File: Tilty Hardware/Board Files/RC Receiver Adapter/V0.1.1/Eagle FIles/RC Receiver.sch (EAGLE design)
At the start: 33 parts, among them J1 AVR_SPI_PRG_6PTH, Q1 16MHz, U1 ATMEGA328P, U2 L298_BRIDGE_DRIVER, U3 LM2931

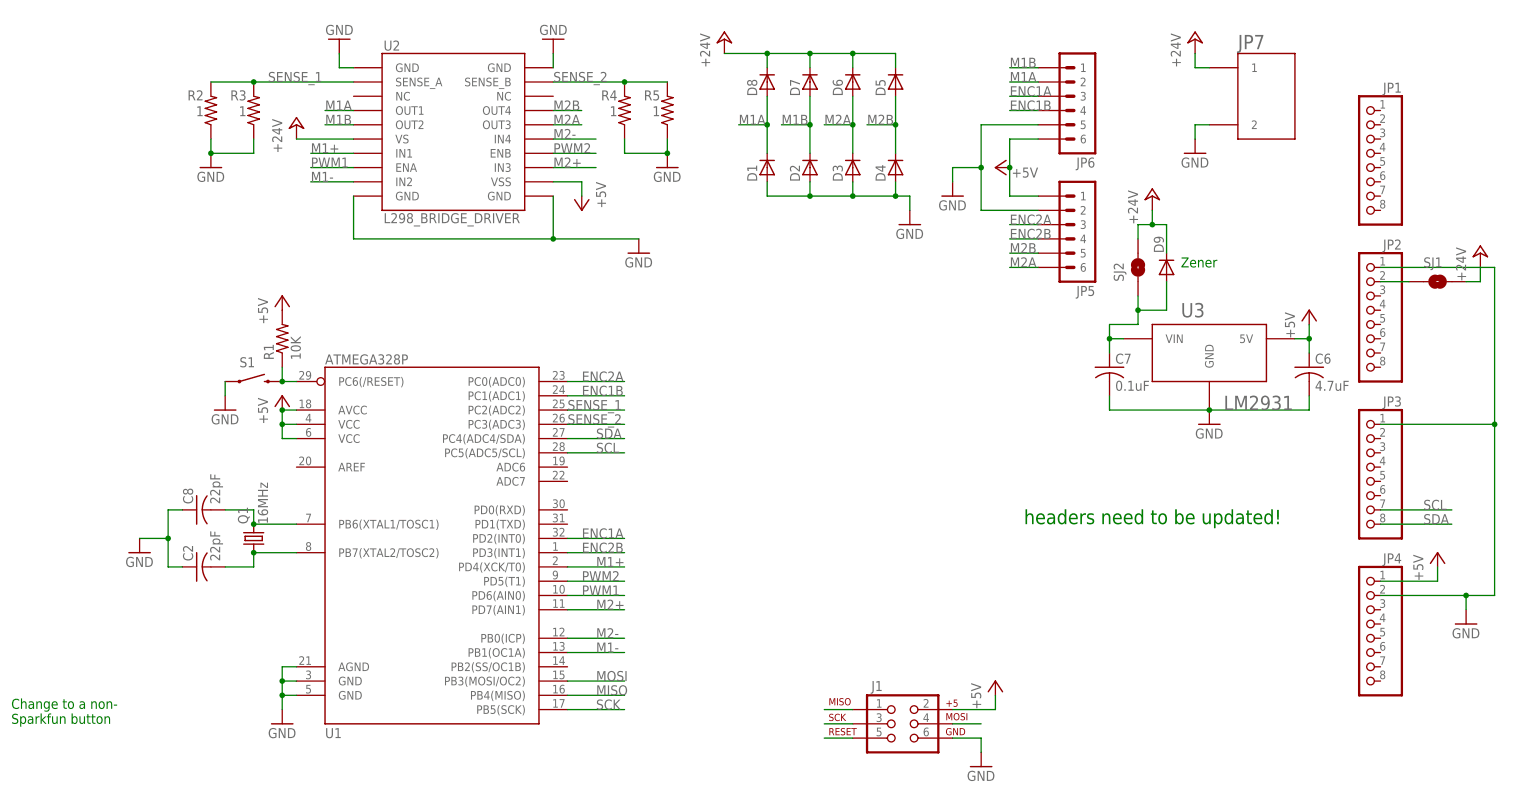
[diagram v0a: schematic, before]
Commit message: New RC Receiver add-on testing code and minor motor driver updates
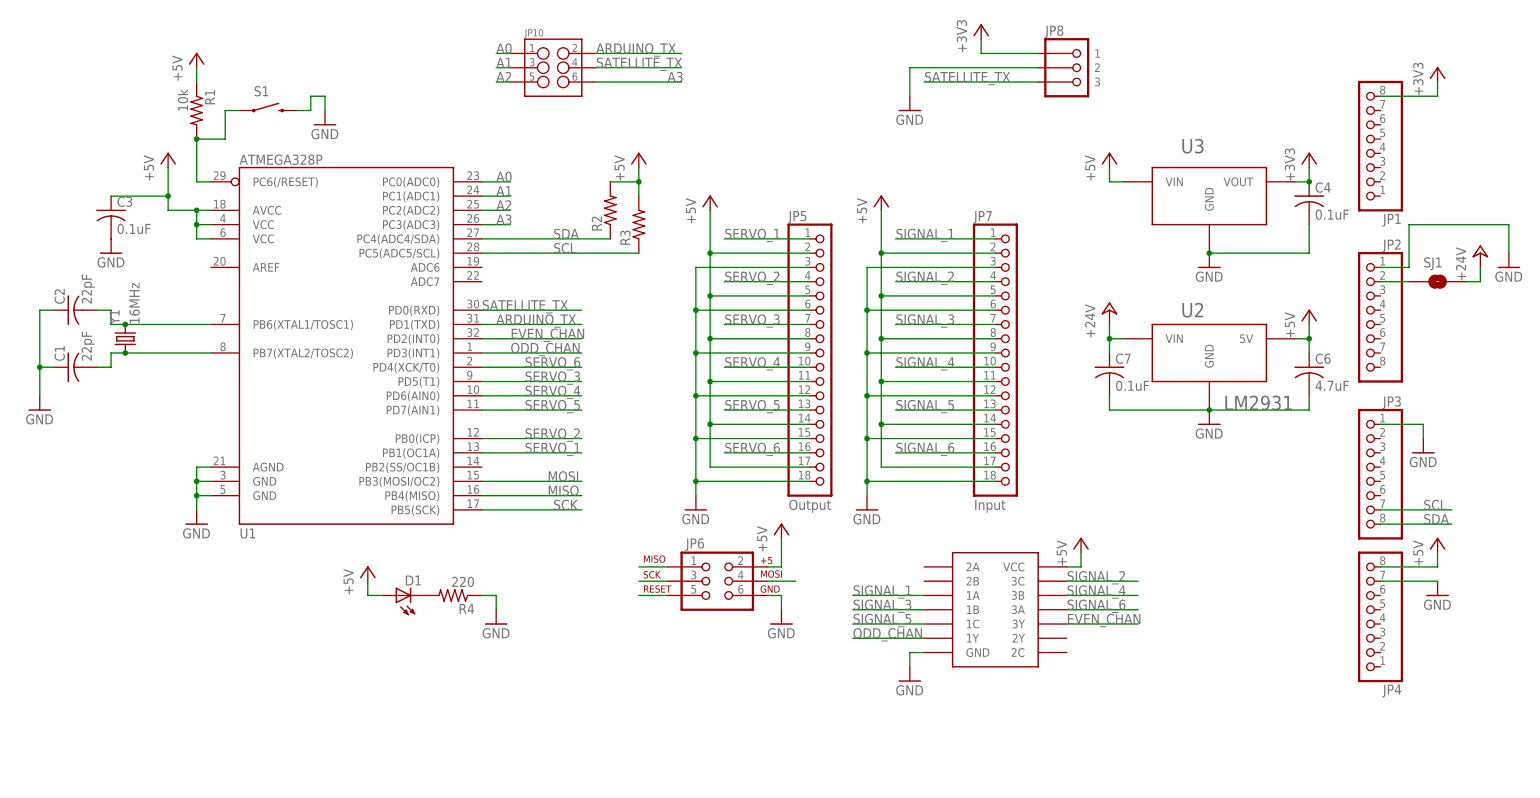
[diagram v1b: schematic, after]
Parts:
- removed C8: 22pF, resistor:C-USC0603
- removed D2, D3, D4, D5, D6, D7, D8: (no value), semicon-smd-ipc:D-SOD123
- removed D9: (no value), diode:DIODE-DO214AA
- removed J1: AVR_SPI_PRG_6PTH, SparkFun-Connectors:AVR_SPI_PRG_6PTH
- removed Q1: 16MHz, crystal:CRYSTALCTS406
- removed R5: 1, resistor:R-US_R0603
- removed SJ2: SOLDERJUMPERTRACE, SparkFun-Passives:SOLDERJUMPERTRACE
- added C1: 22pF, resistor:C-USC0603
- added C3, C4: 0.1uF, resistor:C-USC0603
- added JP10: (no value), SparkFun-Connectors:M03X2NO_SILK
- added JP8: 3-PIN_JST_ZH_PTH_CONNECTORRIGHT_ANGLE_PTH, My Parts:3-PIN_JST_ZH_PTH_CONNECTORRIGHT_ANGLE_PTH
- added U4: C74HC407514-SOIC, My Parts:C74HC407514-SOIC
- added Y1: 16MHz, SparkFun-FreqCtrl:CRYSTAL5X3
- D1: device semicon-smd-ipc:D-SOD123 -> SparkFun-LED:LED-GREENLED-0805_NO_SILK; PART# CDBW140-G -> (none)
- JP5: value 6PIN-SH_RIGHT_ANGLE -> Output; device con-jst:6PIN-SH_RIGHT_ANGLE -> My Parts:18_PIN_HEADER3X6_PTH_HEADER; PART# SM06B-SRSS-TB(LF)(SN) -> (none)
- JP6: value 6PIN-SH_RIGHT_ANGLE -> AVR_SPI_PRG_62X3_LOCK; device con-jst:6PIN-SH_RIGHT_ANGLE -> SparkFun-Connectors:AVR_SPI_PRG_62X3_LOCK; PART# SM06B-SRSS-TB(LF)(SN) -> (none)
- JP7: value 2-POS_SMD_TERM_BLOCK -> Input; device My Parts:2-POS_SMD_TERM_BLOCK -> My Parts:18_PIN_HEADER3X6_PTH_HEADER
- R1: value 10K -> 10k
- R2, R3: value 1 -> (none)
- R4: value 1 -> 220
- U2: value L298_BRIDGE_DRIVER -> LM2931; device SparkFun-PowerIC:L298_BRIDGE_DRIVER -> on-semiconductor:LM2931; PART# (none) -> lm2931
- U3: value LM2931 -> AP7313SOT23R; device on-semiconductor:LM2931 -> My Parts:AP7313SOT23R
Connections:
- removed net ENC1A: JP6.3, U1.PD2(INT0)
- removed net ENC1B: JP6.4, U1.PC1(ADC1)
- removed net ENC2A: JP5.3, U1.PC0(ADC0)
- removed net ENC2B: JP5.4, U1.PD3(INT1)
- removed net M1+: U1.PD4(XCK/T0), U2.IN1
- removed net M1-: U1.PB1(OC1A), U2.IN2
- removed net M1A: D1.C, D8.A, JP6.2, U2.OUT1
- removed net M1B: D2.C, D7.A, JP6.1, U2.OUT2
- removed net M2+: U1.PD7(AIN1), U2.IN3
- removed net M2-: U1.PB0(ICP), U2.IN4
- removed net M2A: D3.C, D6.A, JP5.6, U2.OUT3
- removed net M2B: D4.C, D5.A, JP5.5, U2.OUT4
- removed net N$3: C7.1, D9.A, SJ2.1, U3.VIN
- removed net N$6: C8.2, Q1.2, U1.PB6(XTAL1/TOSC1)
- removed net N$7: C2.2, Q1.1, U1.PB7(XTAL2/TOSC2)
- removed net PWM1: U1.PD6(AIN0), U2.ENA
- removed net PWM2: U1.PD5(T1), U2.ENB
- removed net SENSE_1: R2.2, R3.2, U1.PC2(ADC2), U2.SENSE_A
- removed net SENSE_2: R4.2, R5.2, U1.PC3(ADC3), U2.SENSE_B
- new net +3V3: C4.1, JP1.8, JP8.1, U3.VOUT
- new net A0: JP10.1, U1.PC0(ADC0)
- new net A1: JP10.3, U1.PC1(ADC1)
- new net A2: JP10.5, U1.PC2(ADC2)
- new net A3: JP10.6, U1.PC3(ADC3)
- new net ARDUINO_TX: JP10.2, U1.PD1(TXD)
- new net EVEN_CHAN: U1.PD2(INT0), U4.3Y
- new net N$1: C2.2, U1.PB6(XTAL1/TOSC1), Y1.2
- new net N$2: C1.2, U1.PB7(XTAL2/TOSC2), Y1.1
- new net N$8: D1.C, R4.2
- new net ODD_CHAN: U1.PD3(INT1), U4.1Y
- new net SATELLITE_TX: JP10.4, JP8.3, U1.PD0(RXD)
- new net SERVO_1: JP5.1, U1.PB1(OC1A)
- new net SERVO_2: JP5.4, U1.PB0(ICP)
- new net SERVO_3: JP5.7, U1.PD5(T1)
- new net SERVO_4: JP5.10, U1.PD6(AIN0)
- new net SERVO_5: JP5.13, U1.PD7(AIN1)
- new net SERVO_6: JP5.16, U1.PD4(XCK/T0)
- new net SIGNAL_1: JP7.1, U4.1A
- new net SIGNAL_2: JP7.4, U4.3C
- new net SIGNAL_3: JP7.7, U4.1B
- new net SIGNAL_4: JP7.10, U4.3B
- new net SIGNAL_5: JP7.13, U4.1C
- new net SIGNAL_6: JP7.16, U4.3A
- net +24V: now also C7.1, U2.VIN; no longer D5.C, D6.C, D7.C, D8.C, D9.C, JP7.1, SJ2.2, U2.VS
- net +5V: now also C3.1, D1.A, JP4.8, JP5.11, JP5.14, JP5.17, JP5.2, JP5.5, JP5.8, JP6.2, JP7.11, JP7.14, JP7.17, JP7.2, JP7.5, JP7.8, R1.1, R2.2, R3.2, U2.5V, U3.VIN, U4.VCC; no longer J1.2, JP4.1, JP5.1, JP6.6, R1.2, U2.VSS, U3.5V
- net GND: now also C1.1, C3.2, C4.2, JP4.7, JP5.12, JP5.15, JP5.18, JP5.3, JP5.6, JP5.9, JP6.6, JP7.12, JP7.15, JP7.18, JP7.3, JP7.6, JP7.9, JP8.2, S1.2, U2.GND, U4.GND; no longer C8.1, D1.A, D2.A, D3.A, D4.A, J1.6, JP4.2, JP5.2, JP6.5, JP7.2, R2.1, R3.1, R5.1, S1.1, U2.GND@1, U2.GND@10, U2.GND@11, U2.GND@20
- net MISO: now also JP6.1; no longer J1.1
- net MOSI: now also JP6.4; no longer J1.4
- net RESET: now also JP6.5, R1.2, S1.1; no longer J1.5, R1.1, S1.2
- net SCK: now also JP6.3; no longer J1.3
- net SCL: now also R3.1
- net SDA: now also R2.1
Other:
- note removed: "Change to a non- Sparkfun button"
- note removed: "Zener"
- note removed: "headers need to be updated!"
- moved on the sheet: C2, JP1, JP4, R1, R2, R3, R4, S1, U1, U3

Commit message: R/C Receiver add-on work
fixed OR gate, moved reset button, corrected servo labels
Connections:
- net EVEN_CHAN: now also U1.PD3(INT1), U4.1Y; no longer U1.PD2(INT0), U4.3Y
- net ODD_CHAN: now also U1.PD2(INT0), U4.3Y; no longer U1.PD3(INT1), U4.1Y
- net SIGNAL_1: now also U4.3C; no longer U4.1A
- net SIGNAL_2: now also U4.1A; no longer U4.3C
- net SIGNAL_3: now also U4.3B; no longer U4.1B
- net SIGNAL_4: now also U4.1B; no longer U4.3B
- net SIGNAL_5: now also U4.3A; no longer U4.1C
- net SIGNAL_6: now also U4.1C; no longer U4.3A
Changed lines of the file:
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@@
 </segment>
 <segment>
-<pinref part="U4" gate="G$1" pin="1A"/>
-<wire x1="165.1" y1="27.94" x2="152.4" y2="27.94" width="0.1524" layer="91"/>
-<label x="152.4" y="27.94" size="1.778" layer="95"/>
+<pinref part="U4" gate="G$1" pin="3C"/>
+<wire x1="190.5" y1="30.48" x2="203.2" y2="30.48" width="0.1524" layer="91"/>
+<label x="190.5" y="30.48" size="1.778" layer="95"/>
 </segment>
 </net>
@@
 </segment>
 <segment>
-<pinref part="U4" gate="G$1" pin="3C"/>
-<wire x1="190.5" y1="30.48" x2="203.2" y2="30.48" width="0.1524" layer="91"/>
-<label x="190.5" y="30.48" size="1.778" layer="95"/>
+<pinref part="U4" gate="G$1" pin="1A"/>
+<wire x1="165.1" y1="27.94" x2="152.4" y2="27.94" width="0.1524" layer="91"/>
+<label x="152.4" y="27.94" size="1.778" layer="95"/>
 </segment>
 </net>
@@
 </segment>
 <segment>
-<pinref part="U4" gate="G$1" pin="1B"/>
-<wire x1="165.1" y1="25.4" x2="152.4" y2="25.4" width="0.1524" layer="91"/>
-<label x="152.4" y="25.4" size="1.778" layer="95"/>
+<pinref part="U4" gate="G$1" pin="3B"/>
+<wire x1="190.5" y1="27.94" x2="203.2" y2="27.94" width="0.1524" layer="91"/>
+<label x="190.5" y="27.94" size="1.778" layer="95"/>
 </segment>
 </net>
@@
 </segment>
 <segment>
-<pinref part="U4" gate="G$1" pin="3B"/>
-<wire x1="190.5" y1="27.94" x2="203.2" y2="27.94" width="0.1524" layer="91"/>
-<label x="190.5" y="27.94" size="1.778" layer="95"/>
+<pinref part="U4" gate="G$1" pin="1B"/>
+<wire x1="165.1" y1="25.4" x2="152.4" y2="25.4" width="0.1524" layer="91"/>
+<label x="152.4" y="25.4" size="1.778" layer="95"/>
 </segment>
 </net>
@@
 </segment>
 <segment>
-<pinref part="U4" gate="G$1" pin="1C"/>
-<wire x1="165.1" y1="22.86" x2="152.4" y2="22.86" width="0.1524" layer="91"/>
-<label x="152.4" y="22.86" size="1.778" layer="95"/>
+<pinref part="U4" gate="G$1" pin="3A"/>
+<wire x1="190.5" y1="25.4" x2="203.2" y2="25.4" width="0.1524" layer="91"/>
+<label x="190.5" y="25.4" size="1.778" layer="95"/>
 </segment>
 </net>
@@
 </segment>
 <segment>
-<pinref part="U4" gate="G$1" pin="3A"/>
-<wire x1="190.5" y1="25.4" x2="203.2" y2="25.4" width="0.1524" layer="91"/>
-<label x="190.5" y="25.4" size="1.778" layer="95"/>
+<pinref part="U4" gate="G$1" pin="1C"/>
+<wire x1="165.1" y1="22.86" x2="152.4" y2="22.86" width="0.1524" layer="91"/>
+<label x="152.4" y="22.86" size="1.778" layer="95"/>
 </segment>
 </net>
@@
 <net name="ODD_CHAN" class="0">
 <segment>
+<pinref part="U4" gate="G$1" pin="3Y"/>
+<wire x1="190.5" y1="22.86" x2="203.2" y2="22.86" width="0.1524" layer="91"/>
+<label x="190.5" y="22.86" size="1.778" layer="95"/>
+</segment>
+<segment>
+<pinref part="U1" gate="G$1" pin="PD2(INT0)"/>
+<wire x1="86.36" y1="73.66" x2="104.14" y2="73.66" width="0.1524" layer="91"/>
+<label x="91.44" y="73.66" size="1.778" layer="95"/>
+</segment>
+</net>
+<net name="EVEN_CHAN" class="0">
+<segment>
 <pinref part="U4" gate="G$1" pin="1Y"/>
 <wire x1="165.1" y1="20.32" x2="152.4" y2="20.32" width="0.1524" layer="91"/>
@@
 </segment>
 </net>
-<net name="EVEN_CHAN" class="0">
-<segment>
-<pinref part="U4" gate="G$1" pin="3Y"/>
-<wire x1="190.5" y1="22.86" x2="203.2" y2="22.86" width="0.1524" layer="91"/>
-<label x="190.5" y="22.86" size="1.778" layer="95"/>
-</segment>
-<segment>
-<pinref part="U1" gate="G$1" pin="PD2(INT0)"/>
-<wire x1="86.36" y1="73.66" x2="104.14" y2="73.66" width="0.1524" layer="91"/>
-<label x="91.44" y="73.66" size="1.778" layer="95"/>
-</segment>
-</net>

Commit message: RC Receiver add-on tweaking, updating things.todo handling
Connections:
- removed net A0: JP10.1, U1.PC0(ADC0)
- removed net N$8: D1.C, R4.2
- new net STATUS_LED: D1.A, JP10.1, R4.1, U1.PC0(ADC0)
- net +5V: now also R4.2; no longer D1.A
- net GND: now also D1.C; no longer R4.1
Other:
- moved on the sheet: D1, R4
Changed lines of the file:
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@@
 <instance part="P+9" gate="1" x="127" y="99.06"/>
 <instance part="GND12" gate="1" x="124.46" y="43.18"/>
-<instance part="D1" gate="G$1" x="71.12" y="27.94" rot="R90"/>
+<instance part="D1" gate="G$1" x="81.28" y="27.94" rot="R90"/>
 <instance part="P+10" gate="1" x="66.04" y="33.02"/>
-<instance part="R4" gate="G$1" x="81.28" y="27.94" rot="R180"/>
+<instance part="R4" gate="G$1" x="73.66" y="27.94" rot="R180"/>
 <instance part="GND13" gate="1" x="88.9" y="22.86"/>
 <instance part="GND14" gate="1" x="269.24" y="86.36"/>
@@
 </segment>
 <segment>
-<pinref part="R4" gate="G$1" pin="1"/>
 <pinref part="GND13" gate="1" pin="GND"/>
+<wire x1="88.9" y1="27.94" x2="88.9" y2="25.4" width="0.1524" layer="91"/>
+<pinref part="D1" gate="G$1" pin="C"/>
 <wire x1="86.36" y1="27.94" x2="88.9" y2="27.94" width="0.1524" layer="91"/>
-<wire x1="88.9" y1="27.94" x2="88.9" y2="25.4" width="0.1524" layer="91"/>
 </segment>
 <segment>
@@
 </segment>
 <segment>
-<pinref part="D1" gate="G$1" pin="A"/>
-<wire x1="68.58" y1="27.94" x2="66.04" y2="27.94" width="0.1524" layer="91"/>
 <wire x1="66.04" y1="27.94" x2="66.04" y2="30.48" width="0.1524" layer="91"/>
 <pinref part="P+10" gate="1" pin="+5V"/>
+<pinref part="R4" gate="G$1" pin="2"/>
+<wire x1="66.04" y1="27.94" x2="68.58" y2="27.94" width="0.1524" layer="91"/>
 </segment>
 </net>
@@
 </segment>
 </net>
-<net name="N$8" class="0">
-<segment>
-<pinref part="D1" gate="G$1" pin="C"/>
-<pinref part="R4" gate="G$1" pin="2"/>
-</segment>
-</net>
 <net name="ARDUINO_TX" class="0">
 <segment>
@@
 </segment>
 </net>
-<net name="A0" class="0">
-<segment>
-<pinref part="U1" gate="G$1" pin="PC0(ADC0)"/>
-<wire x1="86.36" y1="101.6" x2="91.44" y2="101.6" width="0.1524" layer="91"/>
-<label x="88.9" y="101.6" size="1.778" layer="95"/>
-</segment>
-<segment>
-<wire x1="91.44" y1="124.46" x2="88.9" y2="124.46" width="0.1524" layer="91"/>
-<pinref part="JP10" gate="G$1" pin="1"/>
-<label x="88.9" y="124.46" size="1.778" layer="95"/>
-</segment>
-</net>
 <net name="A2" class="0">
 <segment>
@@
 </segment>
 </net>
+<net name="STATUS_LED" class="0">
+<segment>
+<pinref part="D1" gate="G$1" pin="A"/>
+<pinref part="R4" gate="G$1" pin="1"/>
+<wire x1="78.74" y1="27.94" x2="78.74" y2="33.02" width="0.1524" layer="91"/>
+<junction x="78.74" y="27.94"/>
+<wire x1="78.74" y1="33.02" x2="93.98" y2="33.02" width="0.1524" layer="91"/>
+<label x="78.74" y="33.02" size="1.778" layer="95"/>
+</segment>
+<segment>
+<pinref part="U1" gate="G$1" pin="PC0(ADC0)"/>
+<wire x1="86.36" y1="101.6" x2="104.14" y2="101.6" width="0.1524" layer="91"/>
+<label x="88.9" y="101.6" size="1.778" layer="95"/>
+</segment>
+<segment>
+<wire x1="91.44" y1="124.46" x2="76.2" y2="124.46" width="0.1524" layer="91"/>
+<pinref part="JP10" gate="G$1" pin="1"/>
+<label x="76.2" y="124.46" size="1.778" layer="95"/>
+</segment>
+</net>

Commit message: Made final revisions to Tilty Omni and R/C Receiver adapter before ordering!
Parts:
- added D2: (no value), SparkFun-LED:LED-GREENLED-0805_NO_SILK
- added R5: 220, resistor:R-US_R0603
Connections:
- new net N$4: D2.A, R5.1
- net +5V: now also R5.2
- net GND: now also D2.C
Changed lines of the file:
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@@
 <part name="JP10" library="SparkFun-Connectors" deviceset="M03X2" device="NO_SILK"/>
 <part name="S1" library="SparkFun-Electromechanical" deviceset="SWITCH-MOMENTARY-2" device="SMD"/>
+<part name="D2" library="SparkFun-LED" deviceset="LED-GREEN" device="LED-0805_NO_SILK"/>
+<part name="R5" library="resistor" deviceset="R-US_" device="R0603" value="220"/>
+<part name="GND16" library="supply1" deviceset="GND" device=""/>
+<part name="P+11" library="supply1" deviceset="+5V" device=""/>
 </parts>
 <sheets>
@@
 <attribute name="NAME" x="45.72" y="116.84" size="1.778" layer="95"/>
 </instance>
+<instance part="D2" gate="G$1" x="45.72" y="27.94" rot="R90"/>
+<instance part="R5" gate="G$1" x="38.1" y="27.94" rot="R180"/>
+<instance part="GND16" gate="1" x="53.34" y="22.86"/>
+<instance part="P+11" gate="1" x="30.48" y="33.02"/>
 </instances>
 <busses>
@@
 <pinref part="GND15" gate="1" pin="GND"/>
 </segment>
+<segment>
+<pinref part="D2" gate="G$1" pin="C"/>
+<wire x1="50.8" y1="27.94" x2="53.34" y2="27.94" width="0.1524" layer="91"/>
+<pinref part="GND16" gate="1" pin="GND"/>
+<wire x1="53.34" y1="27.94" x2="53.34" y2="25.4" width="0.1524" layer="91"/>
+</segment>
 </net>
 <net name="+24V" class="0">
@@
 <wire x1="66.04" y1="27.94" x2="68.58" y2="27.94" width="0.1524" layer="91"/>
 </segment>
+<segment>
+<pinref part="P+11" gate="1" pin="+5V"/>
+<wire x1="30.48" y1="30.48" x2="30.48" y2="27.94" width="0.1524" layer="91"/>
+<pinref part="R5" gate="G$1" pin="2"/>
+<wire x1="30.48" y1="27.94" x2="33.02" y2="27.94" width="0.1524" layer="91"/>
+</segment>
 </net>
 <net name="N$5" class="0">
@@
 </segment>
 </net>
+<net name="N$4" class="0">
+<segment>
+<pinref part="D2" gate="G$1" pin="A"/>
+<pinref part="R5" gate="G$1" pin="1"/>
+</segment>
+</net>
